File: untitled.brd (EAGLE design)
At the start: 43.2 x 14.4 mm, 52 parts, among them J2 1x3 RA Female .1", J3 CORTEX_DEBUG_PTH, J4 USB-MICROB, Q1 BSS123, Q2 BSS123

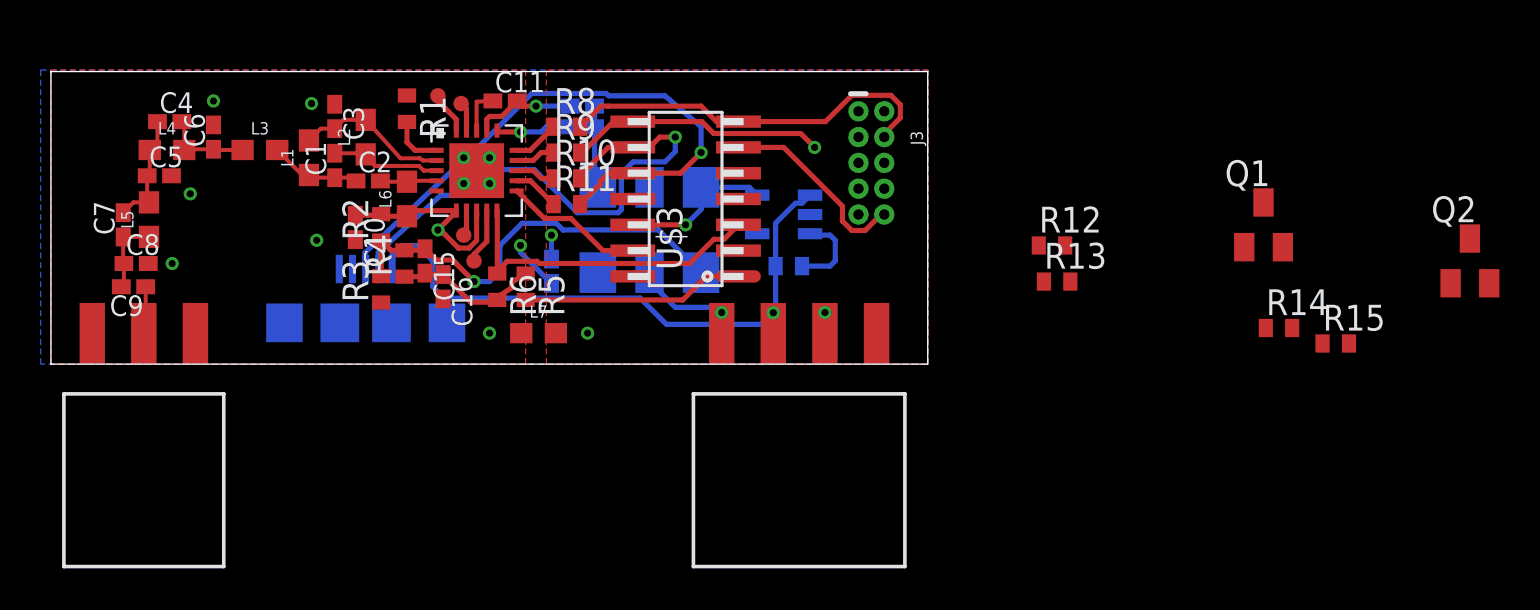
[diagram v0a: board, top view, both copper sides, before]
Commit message: RC1
added 0805 resistor divider package for voltage level conversion of inputs. Final routing pass and verified DRC.
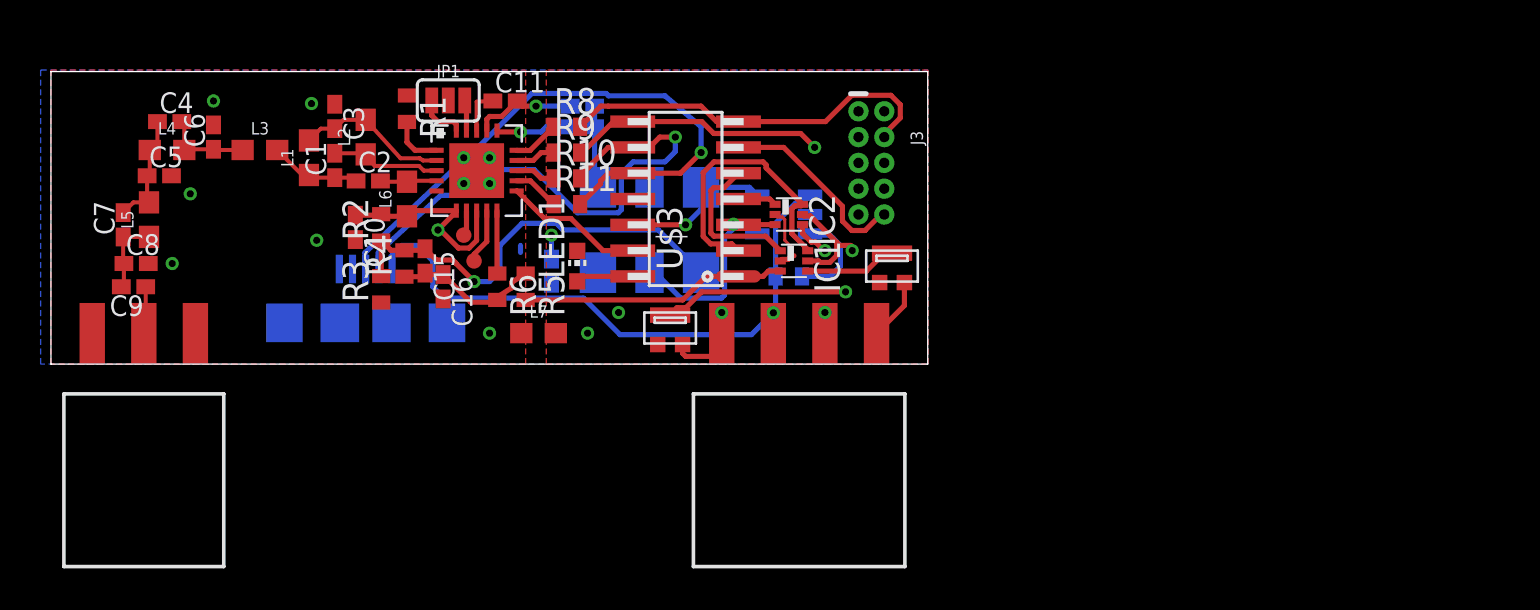
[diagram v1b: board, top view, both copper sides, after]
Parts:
- removed Q1, Q2: BSS123, transistor-small-signal:SOT23
- removed R12, R14: 10k, resistor:R0402
- removed R13, R15: 20k, resistor:R0402
- removed TP4, TP5: TEST-POINT3, SparkFun-Connectors:PAD.03X.03
- added IC1, IC2: 741G3157DRLR, 74xx-little-us:DRL_R-PDSO-N6
- added JP1: JUMPER-SMT_3_NO_SILK, SparkFun-Jumpers:SMT-JUMPER_3_NO_SILK
- added LED1: (no value), adafruit:CHIP-LED0603
- added U$5, U$6: RM20A10K/20K, resistor:RM20A10K/20K
- moved R7 0.51 mm to (36.3, 4.32)
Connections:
- removed net N$7: Q1.3, R13.1
- removed net N$8: Q2.3, R15.1
- removed net PA14: R14.1, R15.2, U$3.4
- new net AUDIO_I2C: IC1.1, U$3.5
- new net AUDIO_IN: J1.4, U$6.P$1
- new net ENABLE_I2C: IC2.1, U$3.4
- new net ENABLE_IN: J1.1, U$5.P$1
- new net ENABLE_IO: IC2.4, U$5.P$3
- net AUDIO: now also IC1.3; no longer R12.2
- net AUDIO_IO: now also IC1.4, U$6.P$3; no longer J1.4, R12.1, R13.2, U$3.5
- net ENABLE: now also IC2.3, U$3.3; no longer J1.1, R14.2
- net GND: now also IC1.2, IC2.2, JP1.2, LED1.C, U$5.P$2, U$6.P$2; no longer Q1.2, Q2.2
- net GPIO2: now also JP1.3; no longer TP4.P$1
- net GPIO3: now also JP1.1; no longer TP5.P$1
- net MODULATION: no longer U$3.3
- net PA04: now also LED1.A; no longer Q1.1, Q2.1
- net PA08: now also IC1.6, IC2.6
- net VCC: now also IC1.5, IC2.5
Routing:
- net ENABLE_IN: track 0.00 -> 19.9 mm, vias 0 -> 1
- net PA08: track 0.00 -> 17.1 mm
- net ENABLE_IO: track 0.00 -> 13.7 mm, vias 0 -> 2
- net MODULATION: track 16.0 -> 3.10 mm
- net AUDIO_I2C: track 0.00 -> 7.58 mm
- net VCC: track 19.2 -> 25.5 mm, vias 3 -> 4
- net ENABLE: track 5.66 -> 10.5 mm
- net AUDIO_IO: track 0.00 -> 4.52 mm
- net AUDIO_IN: track 0.00 -> 3.07 mm
- net PA04: track 0.00 -> 2.83 mm
- net AUDIO: track 11.0 -> 13.1 mm
- net ENABLE_I2C: track 0.00 -> 1.91 mm
- net GND: track 5.62 -> 7.31 mm
- net EN: track 4.13 -> 4.85 mm

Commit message: Updated pin placements
updated pin placements to their correct locations. Moved the ti switch to clear the 10 pin jtag header. adjusted board outline to correct size.
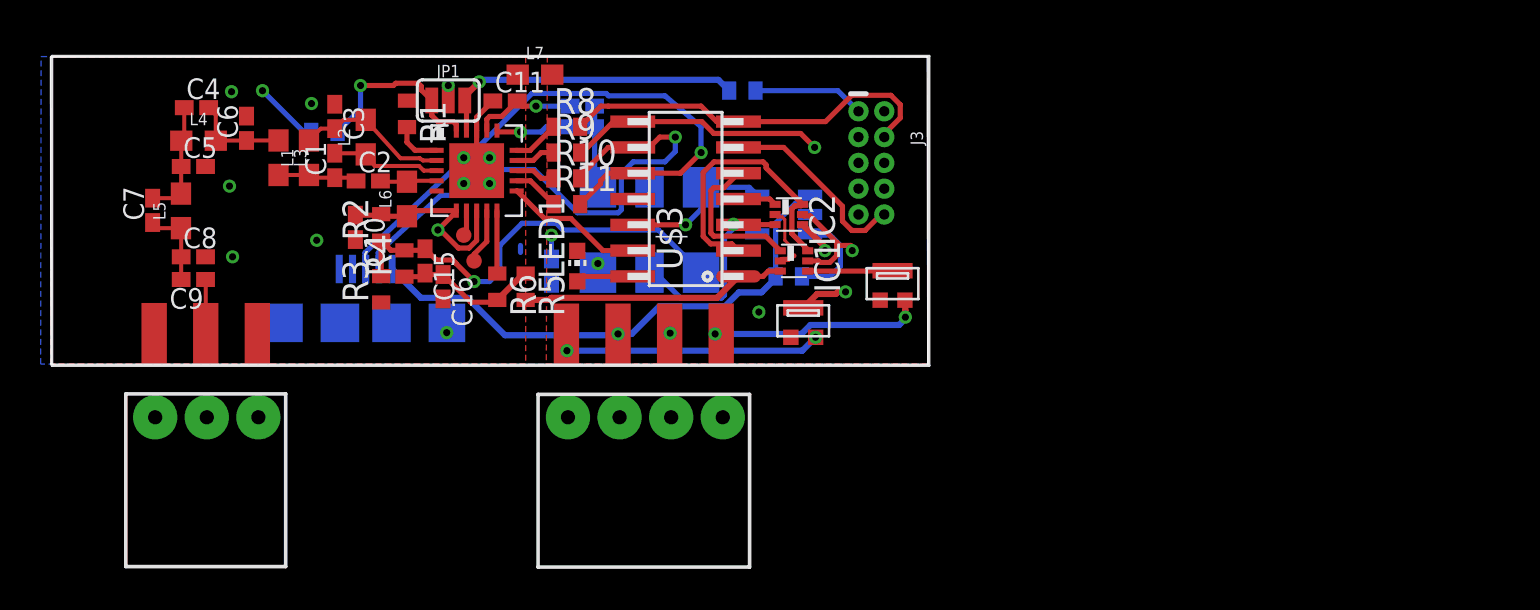
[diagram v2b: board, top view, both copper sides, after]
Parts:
- added R12, R13: 10k, resistor:R0402
- added U$7: RADIOMETRIX-HX1, Ava:RADIOMETRIX-HX1
- moved L7 12.7 mm to (23.8, 14.2)
- moved J1 7.65 mm to (29.2, -5.74)
- moved U$5 6.56 mm to (37.0, 2.13)
- moved J2 3.05 mm to (7.62, -5.71)
- moved C9 2.97 mm to (7.01, 4.17)
- moved C8 2.84 mm to (7.01, 5.28)
- moved C5 1.74 mm to (7.01, 9.73)
- moved C6 1.68 mm to (9.63, 11.6)
- moved L5 1.63 mm to (6.40, 7.54)
- moved L4 1.62 mm to (7.26, 11.0)
- moved C7 1.61 mm to (5.00, 7.57)
- moved C4 1.49 mm to (7.16, 12.6)
- moved L3 0.99 mm to (11.2, 10.2), turned to 270 degrees
- moved U$6 0.86 mm to (41.4, 3.96)
- moved R1 0.25 mm to (17.5, 12.3)
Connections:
- net GPIO2: now also R13.2
- net GPIO3: now also R12.2
- net VCC: now also R12.1, R13.1
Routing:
- net GPIO2: track 1.52 -> 15.3 mm, vias 0 -> 1
- net AUDIO_IN: track 3.07 -> 12.0 mm, vias 0 -> 2
- net VCC: track 25.5 -> 34.3 mm, vias 4 -> 5
- net ENABLE_IO: track 13.7 -> 6.60 mm
- net GPIO3: track 2.43 -> 9.19 mm, vias 0 -> 1
- net ENABLE_IN: track 19.9 -> 13.6 mm, vias 1 -> 2
- net 5V: track 31.3 -> 26.4 mm
- net GND: track 7.31 -> 8.47 mm, vias 13 -> 14
- net N$2: track 4.69 -> 4.11 mm
- net N$1: track 4.35 -> 4.86 mm
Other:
- board size 43.2 x 14.4 mm -> 43.2 x 15.1 mm
